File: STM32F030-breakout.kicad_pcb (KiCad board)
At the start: 2 copper layers, 65.9 x 33.1 mm, 38 parts, among them J1 Conn_01x24, J2 Conn_01x24, J5 TagConnect_TC2030, J6 USB_C_Receptacle_USB2.0, U1 STM32F030C8Tx, U2 MCP1802x-xx02xOT, U3 LP5907MFX-3.3, X1 ASE-xxxMHz, Y1 Crystal

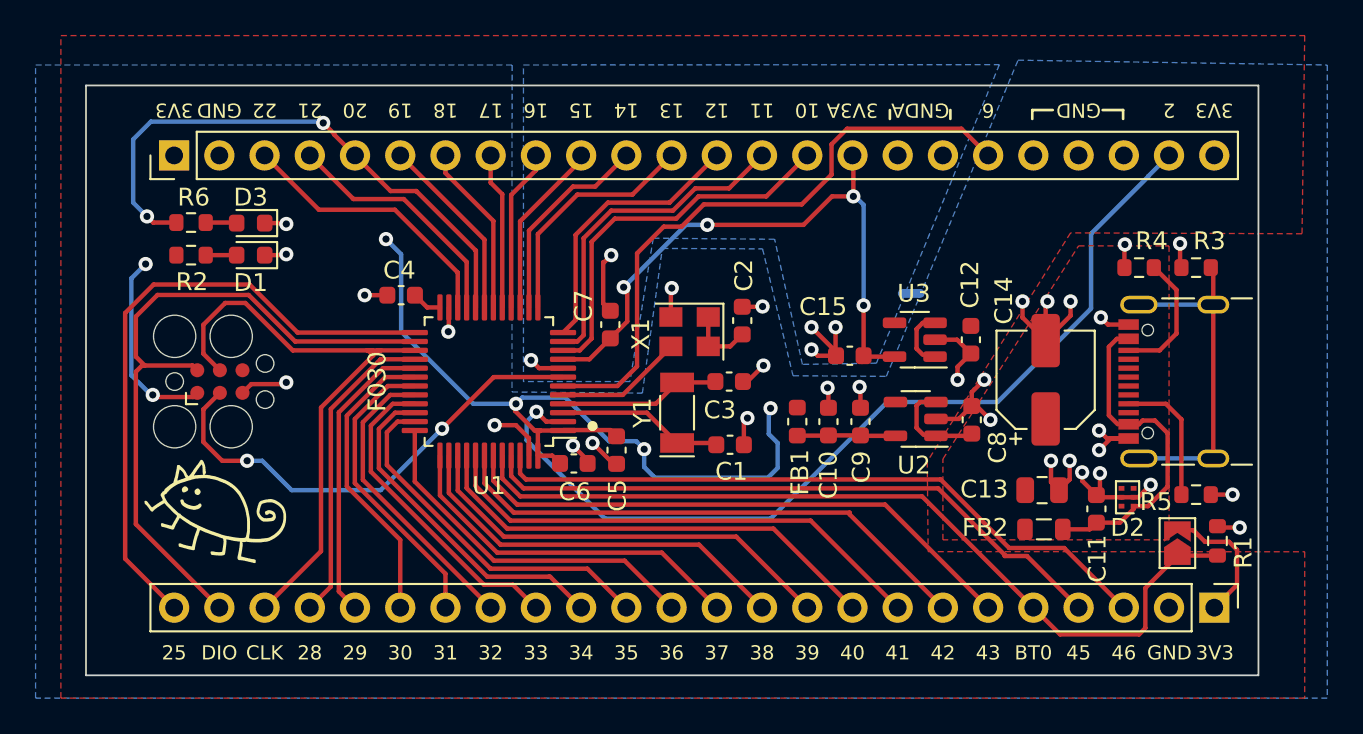
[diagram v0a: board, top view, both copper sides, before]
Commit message: Revision v1: 4-layer board; reset button
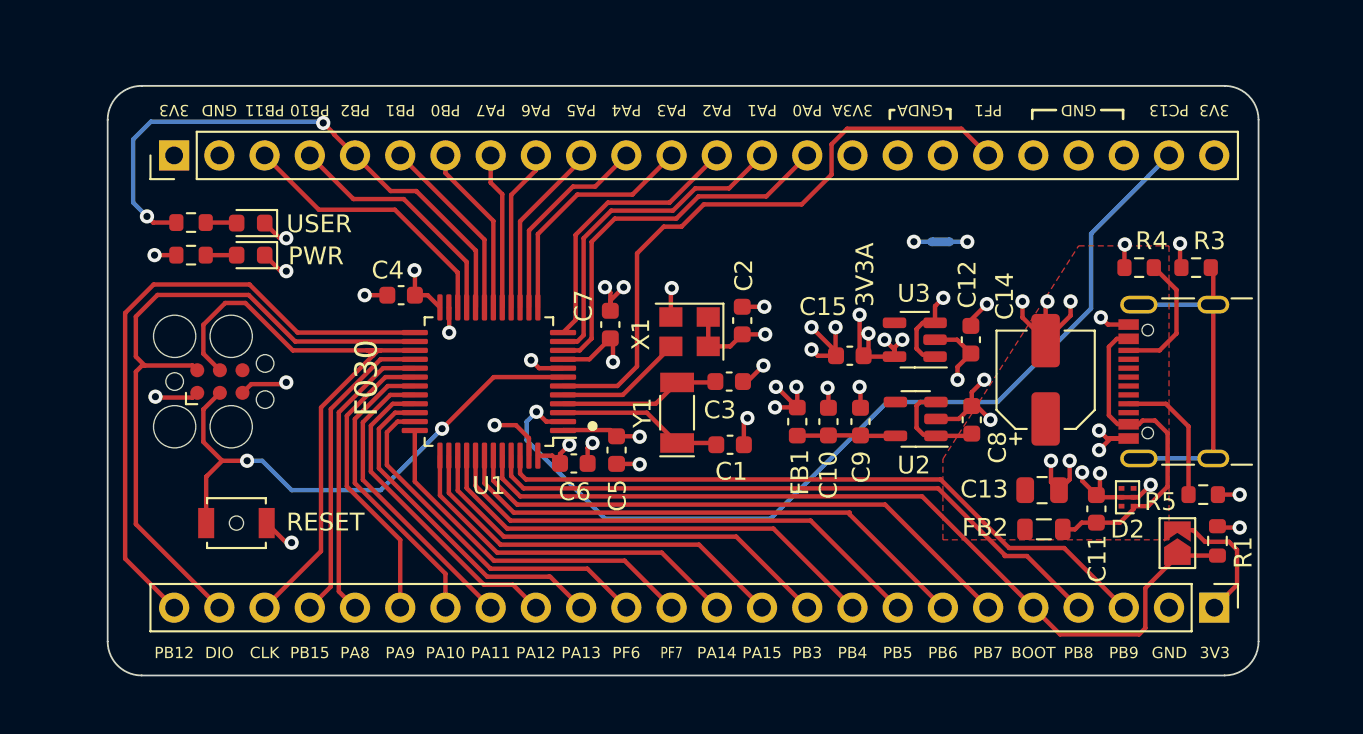
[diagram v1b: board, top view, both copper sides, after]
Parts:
- added Reset1: SW_Push, Button_Switch_SMD:SW_SPST_B3U-1000P-B, F.Cu at (130.5, 84.2)
- G***: moved to B.Cu
- moved G*** 38.7 mm to (167.9, 80.1)
- moved NT1 3.34 mm to (170.1, 68.3)
- moved R5 0.40 mm to (184.8, 82.5)
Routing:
- net +3.3V: track 71.2 -> 36.8 mm, vias 6 -> 11
- net +3.3VA: track 34.8 -> 12.4 mm, vias 4 -> 5
- net /~{RST}: track 27.1 -> 31.0 mm
- net GND: track 60.5 -> 63.6 mm, vias 32 -> 34
- net GNDA: track 10.8 -> 11.4 mm, vias 5 -> 7
- added copper zone on In1.Cu, net +3.3V
- added copper zone on In1.Cu, net +3.3VA
- added copper zone on In2.Cu, net GND
- added copper zone on In2.Cu, net GNDA
- removed copper zone on F.Cu, net +3.3V
- removed copper zone on B.Cu, net GND
- removed copper zone on B.Cu, net GNDA
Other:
- board size 65.9 x 33.1 mm -> 64.6 x 33.1 mm
- copper layers 2 -> 4
- board text added: "BOOT"
- board text added: "Jed Parsons github.com/jedp/ STM32F030-breakout v1"
- board text added: "PA0"
- board text added: "PA1"
- board text added: "PA10"
- board text added: "PA11"
- board text added: "PA12"
- board text added: "PA13"
- board text added: "PA14"
- board text added: "PA15"
- board text added: "PA2"
- board text added: "PA3"
- board text added: "PA4"
- board text added: "PA5"
- board text added: "PA6"
- board text added: "PA7"
- board text added: "PA8"
- board text added: "PA9"
- board text added: "PB0"
- board text added: "PB1"
- board text added: "PB10"
- board text added: "PB11"
- board text added: "PB12"
- board text added: "PB15"
- board text added: "PB2"
- board text added: "PB3"
- board text added: "PB4"
- board text added: "PB5"
- board text added: "PB6"
- board text added: "PB7"
- board text added: "PB8"
- board text added: "PB9"
- board text added: "PC13"
- board text added: "PF1"
- board text added: "PF6"
- board text added: "PF7"
- board text added: "PWR"
- board text added: "RESET"
- board text added: "USER"
- board text removed: "10"
- board text removed: "11"
- board text removed: "12"
- board text removed: "13"
- board text removed: "14"
- board text removed: "15"
- board text removed: "16"
- board text removed: "17"
- board text removed: "18"
- board text removed: "19"
- board text removed: "2"
- board text removed: "20"
- board text removed: "21"
- board text removed: "22"
- board text removed: "25"
- board text removed: "28"
- board text removed: "29"
- board text removed: "30"
- board text removed: "31"
- board text removed: "32"
- board text removed: "33"
- board text removed: "34"
- board text removed: "35"
- board text removed: "36"
- board text removed: "37"
- board text removed: "38"
- board text removed: "39"
- board text removed: "40"
- board text removed: "41"
- board text removed: "42"
- board text removed: "43"
- board text removed: "45"
- board text removed: "46"
- board text removed: "6"
- board text removed: "BT0"
- board text removed: "Jed Parsons github.com/jedp/"

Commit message: Oof. SWDIO and SWCLK were on the wrong bank.
I made the mistake of swapping out a different F030 symbol in Kicad. Turns out
the A and B ports were swapped!
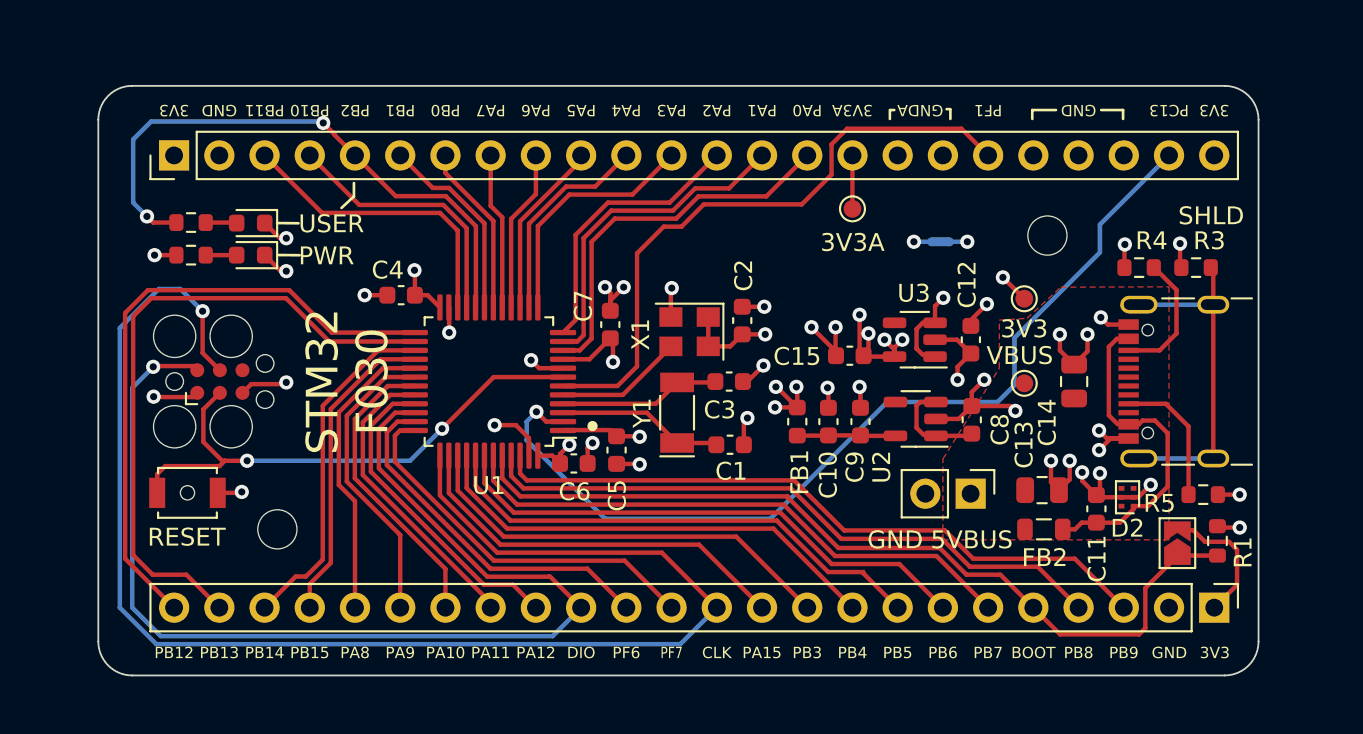
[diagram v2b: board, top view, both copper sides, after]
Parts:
- added H1: MountingHole, MountingHole:MountingHole_2.2mm_M2, F.Cu at (176.1, 68.0)
- added H2: MountingHole, MountingHole:MountingHole_2.2mm_M2, F.Cu at (132.8, 84.5)
- added J3: Conn_01x02_Female, Connector_PinHeader_2.54mm:PinHeader_1x02_P2.54mm_Vertical, F.Cu at (171.7, 82.5)
- added TP1: TestPoint, TestPoint:TestPoint_Pad_D1.0mm, F.Cu at (165.1, 66.5)
- added TP2: TestPoint, TestPoint:TestPoint_Pad_D1.0mm, F.Cu at (174.8, 76.3)
- added TP3: TestPoint, TestPoint:TestPoint_Pad_D1.0mm, F.Cu at (174.8, 71.5)
- C14: footprint Capacitor_SMD:CP_Elec_5x3 -> Capacitor_SMD:C_0805_2012Metric
- moved G*** 10.7 mm to (178.1, 76.5)
- moved Reset1 3.23 mm to (127.8, 82.5)
- moved C14 1.60 mm to (177.6, 76.2)
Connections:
- J2 pad 12: /PA14 -> /SWCLK
- J2 pad 15: /PA13 -> /SWDIO
- J2 pad 22: /SWCLK -> /PB14
- J2 pad 23: /SWDIO -> /PB13
- U1 pad 26: /SWDIO -> /PB13
- U1 pad 27: /SWCLK -> /PB14
- U1 pad 34: /PA13 -> /SWDIO
- U1 pad 37: /PA14 -> /SWCLK
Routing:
- net /SWCLK: track 34.3 -> 81.1 mm, vias 0 -> 1
- net /PB13: track 0.00 -> 36.7 mm
- net /SWDIO: track 39.1 -> 62.3 mm, vias 0 -> 1
- net /PA14: track 20.4 -> 0.00 mm
- net /PB14: track 0.00 -> 19.5 mm
- net /PA13: track 19.2 -> 0.00 mm
- net GND: track 63.6 -> 60.6 mm, vias 34 -> 33
- net +3.3VA: track 12.4 -> 15.4 mm
- net +3.3V: track 36.8 -> 38.5 mm, vias 11 -> 12
- net GNDA: track 11.4 -> 9.84 mm, vias 7 -> 6
- net /PF7: track 20.2 -> 21.6 mm
- net /PB11: track 15.5 -> 16.9 mm
- net /PB10: track 13.8 -> 15.0 mm
- net /LED_USER: track 32.3 -> 33.1 mm
- net /PB1: track 10.5 -> 11.0 mm
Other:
- board size 64.6 x 33.1 mm -> 65.2 x 33.1 mm
- board text added: "5VBUS"
- board text added: "PB13"
- board text added: "PB14"
- board text added: "SHLD"
- board text added: "STM32"
- board text added: "VBUS"
- board text removed: "PA13"
- board text removed: "PA14"

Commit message: Move oscillators closer
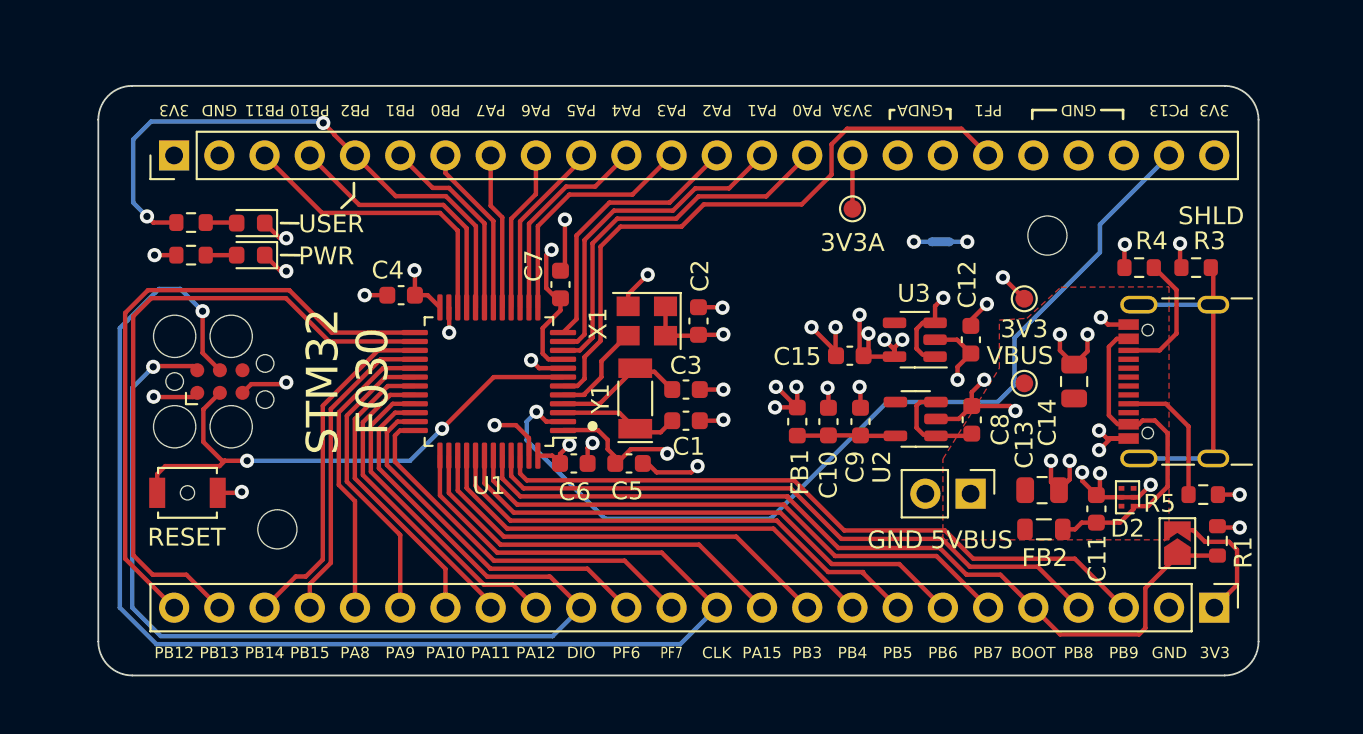
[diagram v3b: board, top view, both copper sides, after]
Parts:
- moved C7 3.59 mm to (148.7, 70.8)
- moved C1 2.82 mm to (155.8, 78.4)
- moved Y1 2.48 mm to (152.9, 77.2)
- moved X1 2.47 mm to (153.6, 72.8)
- moved C3 2.47 mm to (155.8, 76.7)
- moved C2 2.46 mm to (156.4, 72.8)
- moved C5 1.03 mm to (152.6, 80.8), turned to 0 degrees
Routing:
- net +3.3VA: track 15.4 -> 18.9 mm
- net +3.3V: track 38.5 -> 41.5 mm
- net /LSE_XA: track 9.35 -> 6.77 mm
- net GND: track 60.6 -> 63.0 mm
- net /LSE_XB: track 9.08 -> 7.38 mm
- net /HSE_IN: track 7.20 -> 5.59 mm
- net GNDA: track 9.84 -> 9.74 mm, vias 6 -> 5
